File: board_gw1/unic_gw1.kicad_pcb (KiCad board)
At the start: 4 copper layers, 50 x 15.2 mm, 127 parts, among them Q1 2N7002, Q10 2N7002, Q11 2N7002, Q12 2N7002, Q13 2N7002, Q14 2N7002, Q15 2N7002, Q16 2N7002, Q17 2N7002, Q18 2N7002, Q19 2N7002, Q2 2N7002, Q20 2N7002, Q21 2N7002, Q22 2N7002, Q23 2N7002, Q24 2N7002, Q25 2N7002, Q26 2N7002, Q27 2N7002, Q28 2N7002, Q29 2N7002, Q3 2N7002, Q30 2N7002, Q31 2N7002, Q32 2N7002, Q33 2N7002, Q34 2N7002, Q35 2N7002, Q36 2N7002, Q37 2N7002, Q38 2N7002, Q39 2N7002, Q4 2N7002, Q40 2N7002, Q41 2N7002, Q5 2N7002, Q6 2N7002, Q7 2N7002, Q8 2N7002, Q9 2N7002, U1 GW1N-LV9QN88C6_I5_, U3 MIC5203-3.3BM5, U4 APS6404L-3SQR-ZR, U5 MIC5504-1.2YM5, U6 AP62150Z6, U7 W25Q16JVUXIQ, X1 27MHz

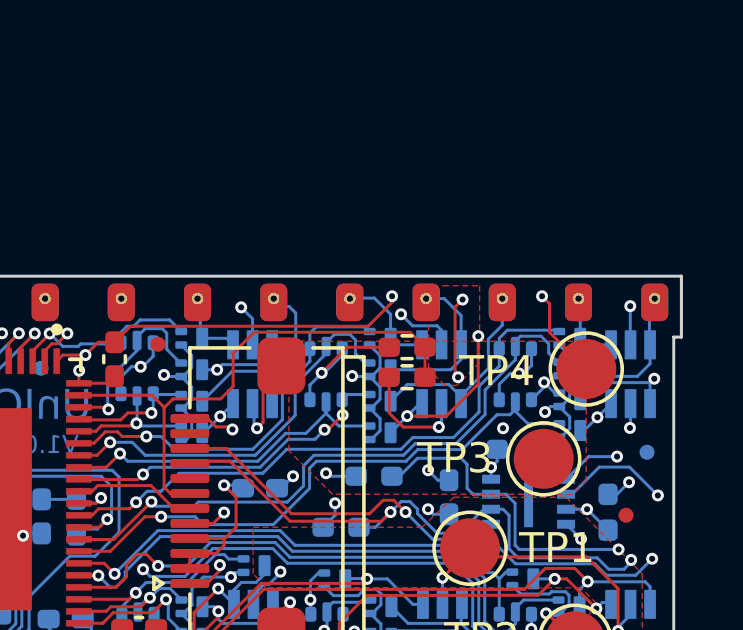
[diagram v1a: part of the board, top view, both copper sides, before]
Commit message: Changed PCB to match that of manufacturing:
1. Removed solder paste from U1 (as it will be hand-soldered).
2. Changed vias to have pads on top/bottom.
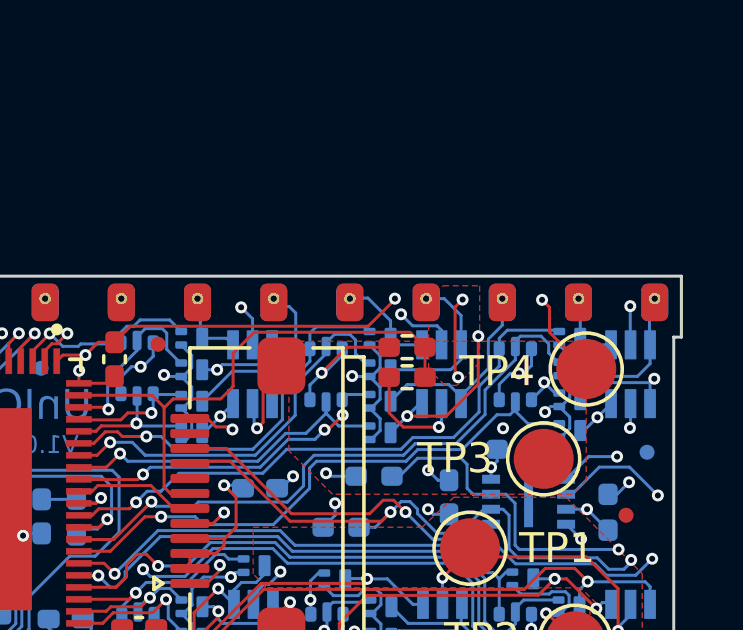
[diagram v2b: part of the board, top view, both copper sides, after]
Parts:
- U1: value GW1N-LV9QN88C6_I5_ -> GW1NR-LV9-QN88-C6/I5

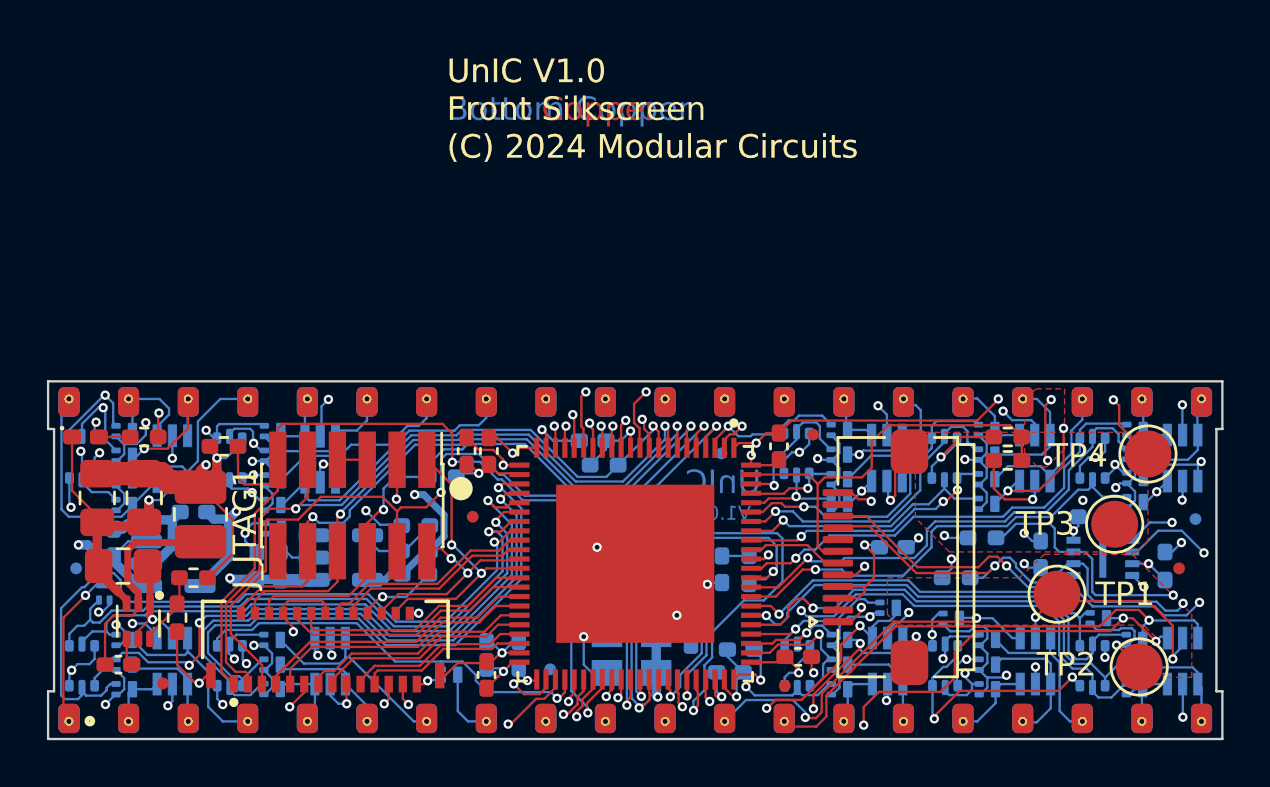
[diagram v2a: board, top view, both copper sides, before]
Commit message: New diodes are added
PCB is also fixed up, but fab notes
need cleaning. Also, I need to select
an actual diode.
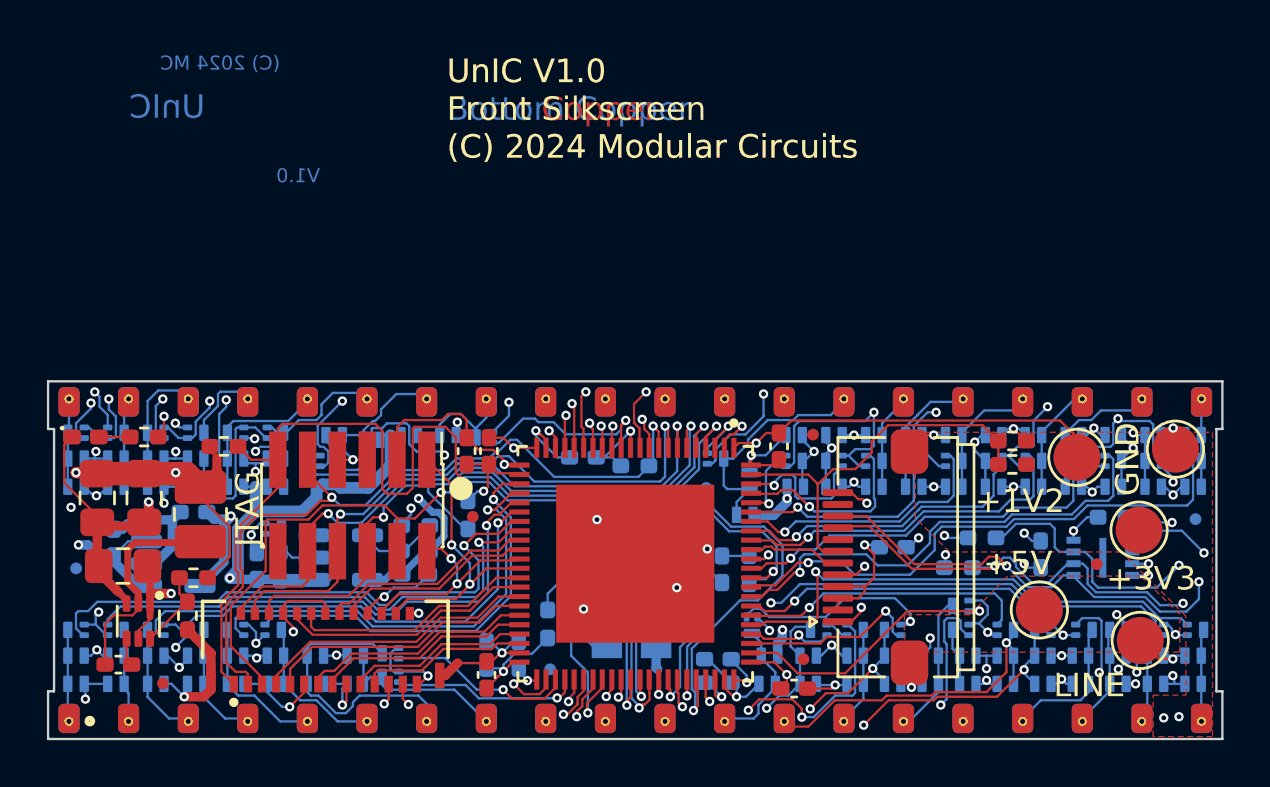
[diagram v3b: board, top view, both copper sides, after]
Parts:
- removed D21, D22, D23, D24, D25, D26, D27, D28, D29, D30: BAT54CV, UNIC:SOT-666
- added D10: D_Schottky, Diode_SMD:D_SOD-882, B.Cu at (70.7, 68.0)
- added D12: D_Schottky, Diode_SMD:D_SOD-882, B.Cu at (70.7, 66.8)
- added D13: D_Schottky, Diode_SMD:D_SOD-882, B.Cu at (46.3, 68.0)
- added D14: D_Schottky, Diode_SMD:D_SOD-882, B.Cu at (48.0, 66.8)
- added D15: D_Schottky, Diode_SMD:D_SOD-882, B.Cu at (48.0, 68.0)
- added D16: D_Schottky, Diode_SMD:D_SOD-882, B.Cu at (80.7, 66.8)
- added D17: D_Schottky, Diode_SMD:D_SOD-882, B.Cu at (80.7, 68.0)
- added D18: D_Schottky, Diode_SMD:D_SOD-882, B.Cu at (79.1, 66.8)
- added D19: D_Schottky, Diode_SMD:D_SOD-882, B.Cu at (79.1, 68.0)
- added D20: D_Schottky, Diode_SMD:D_SOD-882, B.Cu at (87.1, 66.8)
- added D31: D_Schottky, Diode_SMD:D_SOD-882, B.Cu at (87.1, 68.0)
- added D32: D_Schottky, Diode_SMD:D_SOD-882, B.Cu at (85.5, 66.8)
- added D33: D_Schottky, Diode_SMD:D_SOD-882, B.Cu at (85.5, 68.0)
- added D34: D_Schottky, Diode_SMD:D_SOD-882, B.Cu at (74.3, 66.8)
- added D35: D_Schottky, Diode_SMD:D_SOD-882, B.Cu at (74.3, 68.0)
- added D36: D_Schottky, Diode_SMD:D_SOD-882, B.Cu at (70.1, 59.6)
- added D37: D_Schottky, Diode_SMD:D_SOD-882, B.Cu at (70.1, 57.4)
- added D38: D_Schottky, Diode_SMD:D_SOD-882, B.Cu at (87.1, 59.6)
- added D39: D_Schottky, Diode_SMD:D_SOD-882, B.Cu at (87.1, 57.4)
- added D40: D_Schottky, Diode_SMD:D_SOD-882, B.Cu at (72.7, 66.8)
- added D41: D_Schottky, Diode_SMD:D_SOD-882, B.Cu at (72.7, 68.0)
- added D42: D_Schottky, Diode_SMD:D_SOD-882, B.Cu at (44.6, 68.0)
- added D43: D_Schottky, Diode_SMD:D_SOD-882, B.Cu at (42.9, 66.8)
- added D44: D_Schottky, Diode_SMD:D_SOD-882, B.Cu at (42.9, 68.0)
- added D45: D_Schottky, Diode_SMD:D_SOD-882, B.Cu at (69.0, 66.8)
- added D46: D_Schottky, Diode_SMD:D_SOD-882, B.Cu at (68.9, 68.0)
- added D47: D_Schottky, Diode_SMD:D_SOD-882, B.Cu at (85.4, 59.6)
- added D48: D_Schottky, Diode_SMD:D_SOD-882, B.Cu at (85.4, 57.4)
- added D49: D_Schottky, Diode_SMD:D_SOD-882, B.Cu at (46.3, 59.6)
- added D50: D_Schottky, Diode_SMD:D_SOD-882, B.Cu at (46.3, 58.4)
- added D51: D_Schottky, Diode_SMD:D_SOD-882, B.Cu at (48.0, 59.6)
- added D52: D_Schottky, Diode_SMD:D_SOD-882, B.Cu at (48.0, 58.4)
- added D53: D_Schottky, Diode_SMD:D_SOD-882, B.Cu at (83.7, 59.6)
- added D54: D_Schottky, Diode_SMD:D_SOD-882, B.Cu at (83.7, 57.4)
- added D55: D_Schottky, Diode_SMD:D_SOD-882, B.Cu at (83.9, 66.8)
- added D56: D_Schottky, Diode_SMD:D_SOD-882, B.Cu at (83.9, 68.0)
- added D57: D_Schottky, Diode_SMD:D_SOD-882, B.Cu at (41.2, 66.8)
- added D58: D_Schottky, Diode_SMD:D_SOD-882, B.Cu at (41.2, 68.0)
- added D59: D_Schottky, Diode_SMD:D_SOD-882, B.Cu at (51.4, 66.8)
- added D60: D_Schottky, Diode_SMD:D_SOD-882, B.Cu at (51.4, 68.0)
- added D61: D_Schottky, Diode_SMD:D_SOD-882, B.Cu at (82.3, 66.8)
- added D62: D_Schottky, Diode_SMD:D_SOD-882, B.Cu at (82.3, 68.0)
- added D63: D_Schottky, Diode_SMD:D_SOD-882, B.Cu at (75.2, 59.6)
- added D64: D_Schottky, Diode_SMD:D_SOD-882, B.Cu at (75.2, 57.4)
- added D65: D_Schottky, Diode_SMD:D_SOD-882, B.Cu at (52.1, 57.6)
- added D66: D_Schottky, Diode_SMD:D_SOD-882, B.Cu at (50.5, 57.4)
- added D67: D_Schottky, Diode_SMD:D_SOD-882, B.Cu at (53.7, 57.4)
- added D68: D_Schottky, Diode_SMD:D_SOD-882, B.Cu at (55.3, 57.4)
- added D69: D_Schottky, Diode_SMD:D_SOD-882, B.Cu at (76.9, 59.6)
- added D70: D_Schottky, Diode_SMD:D_SOD-882, B.Cu at (76.9, 57.4)
- added D71: D_Schottky, Diode_SMD:D_SOD-882, B.Cu at (77.5, 66.8)
- added D72: D_Schottky, Diode_SMD:D_SOD-882, B.Cu at (77.5, 68.0)
- added D73: D_Schottky, Diode_SMD:D_SOD-882, B.Cu at (49.7, 66.8)
- added D74: D_Schottky, Diode_SMD:D_SOD-882, B.Cu at (49.7, 68.0)
- added D75: D_Schottky, Diode_SMD:D_SOD-882, B.Cu at (80.3, 59.6)
- added D76: D_Schottky, Diode_SMD:D_SOD-882, B.Cu at (80.3, 57.4)
- added D77: D_Schottky, Diode_SMD:D_SOD-882, B.Cu at (41.2, 59.6)
- added D78: D_Schottky, Diode_SMD:D_SOD-882, B.Cu at (41.2, 58.4)
- added D79: D_Schottky, Diode_SMD:D_SOD-882, B.Cu at (42.9, 59.6)
- added D80: D_Schottky, Diode_SMD:D_SOD-882, B.Cu at (42.9, 58.4)
- added D81: D_Schottky, Diode_SMD:D_SOD-882, B.Cu at (44.6, 59.6)
- added D82: D_Schottky, Diode_SMD:D_SOD-882, B.Cu at (44.6, 58.4)
- added D83: D_Schottky, Diode_SMD:D_SOD-882, B.Cu at (68.0, 60.8)
- added D84: D_Schottky, Diode_SMD:D_SOD-882, B.Cu at (68.2, 59.3)
- added D85: D_Schottky, Diode_SMD:D_SOD-882, B.Cu at (78.6, 59.6)
- added D86: D_Schottky, Diode_SMD:D_SOD-882, B.Cu at (78.6, 57.4)
- added D87: D_Schottky, Diode_SMD:D_SOD-882, B.Cu at (71.8, 59.6)
- added D88: D_Schottky, Diode_SMD:D_SOD-882, B.Cu at (71.8, 57.4)
- added D89: D_Schottky, Diode_SMD:D_SOD-882, B.Cu at (39.5, 59.6)
- added D90: D_Schottky, Diode_SMD:D_SOD-882, B.Cu at (39.5, 58.4)
- added TP5: TestPoint, UNIC:TestPoint_Pad_D2.0mm, F.Cu at (86.3, 58.0)
- D1, D11, D2, D3, D4, D5, D6, D7, D8, D9: value BAT54DF -> D_Schottky; footprint UNIC:SOT65P210X110-6N -> Diode_SMD:D_SOD-882
- moved D5 40.4 mm to (46.3, 66.8), turned to 180 degrees
- moved D3 34.6 mm to (39.5, 68.0), turned to 0 degrees
- moved D8 32.1 mm to (82.0, 57.4), turned to 0 degrees
- moved D9 29.9 mm to (73.5, 59.6), turned to 0 degrees
- moved R9 26.4 mm to (59.6, 65.4), turned to 90 degrees
- moved D11 13.2 mm to (73.5, 57.4), turned to 180 degrees
- moved D2 10.8 mm to (39.5, 66.8), turned to 180 degrees
- moved D6 10.6 mm to (75.9, 68.0), turned to 180 degrees
- moved Q36 9.47 mm to (56.9, 57.5), turned to 180 degrees
- moved Q15 8.50 mm to (68.3, 65.5), turned to -90 degrees
- moved D7 8.04 mm to (82.0, 59.6), turned to 180 degrees
- moved Q13 5.74 mm to (77.2, 64.6), turned to 180 degrees
- moved Q16 5.58 mm to (83.9, 65.7), turned to 180 degrees
- moved Q20 5.52 mm to (79.1, 65.7)
- moved Q29 5.42 mm to (66.7, 58.4)
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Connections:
- D1 pad 1: /PIN1 -> LINE
- D1 pad 2: LINE -> /PIN4
- D11 pad 1: /PIN22 -> /PIN26
- D11 pad 2: LINE -> GND
- D2 pad 1: /PIN8 -> LINE
- D2 pad 2: LINE -> /PIN1
- D3 pad 1: /PIN9 -> /PIN1
- D3 pad 2: LINE -> GND
- D4 pad 1: /PIN12 -> LINE
- D4 pad 2: LINE -> /PIN15
- D5 pad 1: /PIN11 -> LINE
- D5 pad 2: LINE -> /PIN5
- D6 pad 1: /PIN25 -> /PIN15
- D6 pad 2: LINE -> GND
- D7 pad 1: /PIN27 -> LINE
- D7 pad 2: LINE -> /PIN22
- D8 pad 1: /PIN36 -> /PIN22
- D8 pad 2: LINE -> GND
- D9 pad 1: /PIN39 -> LINE
- D9 pad 2: LINE -> /PIN26
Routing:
- net +5V: track 57.5 -> 82.5 mm, vias 15 -> 20
- net +3V3: track 85.4 -> 61.8 mm, vias 29 -> 19
- net GND: track 81.5 -> 100.8 mm, vias 37 -> 44
- net /PIN33_F: track 21.2 -> 7.98 mm, vias 2 -> 1
- net /PIN12: track 16.7 -> 5.66 mm, vias 2 -> 0
- net /PIN7_F: track 18.0 -> 7.61 mm, vias 2 -> 1
- net /PIN8_F: track 17.8 -> 8.02 mm
- net /PIN2_F: track 30.9 -> 21.2 mm
- net /PIN18_F: track 21.6 -> 30.7 mm
- net /PIN12_F: track 22.0 -> 13.0 mm
- net /PIN13: track 21.8 -> 14.0 mm
- net /PIN17_F: track 19.8 -> 27.5 mm
- net /PIN27: track 2.28 -> 9.86 mm
- net /PIN13_F: track 19.7 -> 12.3 mm
- net /PIN6_F: track 24.8 -> 17.5 mm
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- added copper zone on F.Cu, net +5V
- removed copper zone on F.Cu, net LINE
- removed copper zone on In1.Cu, net LINE
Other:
- board text added: "+1V2"
- board text added: "+3V3"
- board text added: "+5V"
- board text added: "GND"
- board text added: "JTAG"
- board text added: "LINE"

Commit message: Updated diode part and footprint.
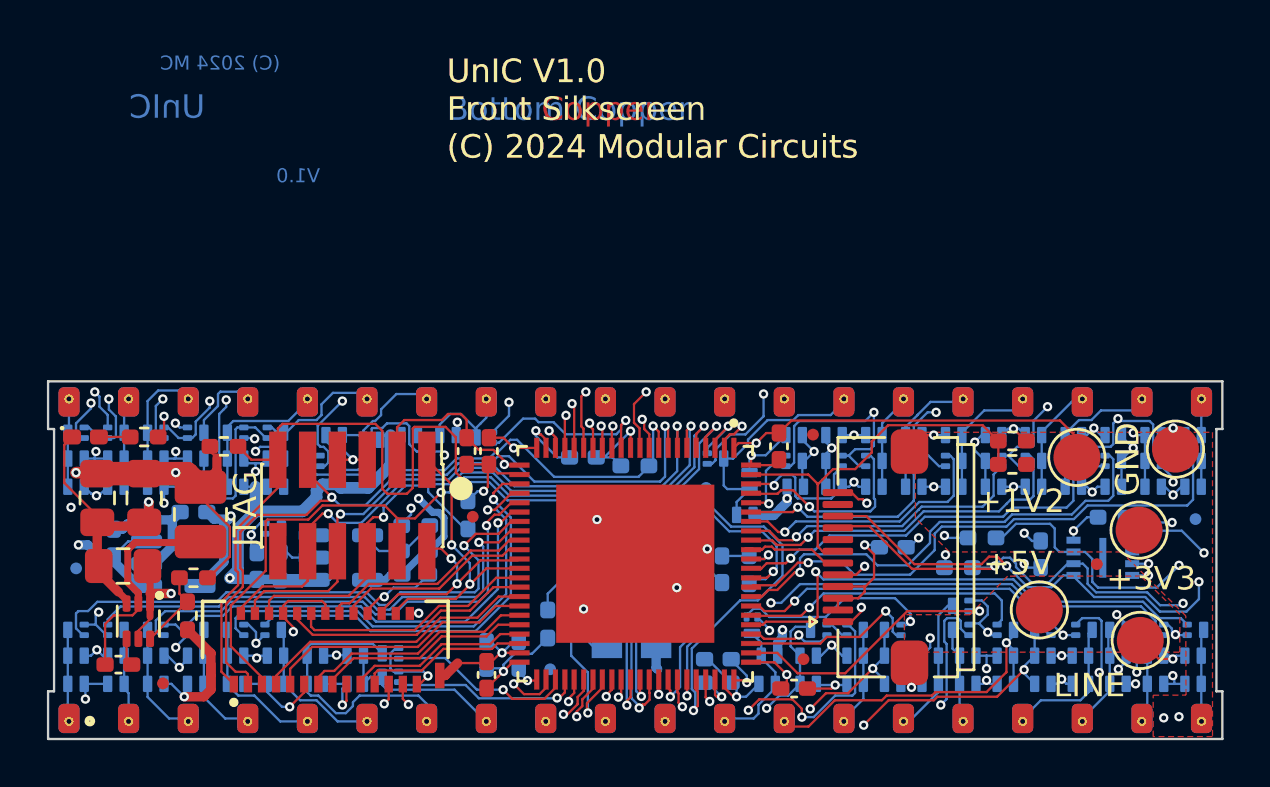
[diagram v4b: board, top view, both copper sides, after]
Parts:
- D1, D10, D11, D12, D13, D14, D15, D16, D17, D18, D19, D2, D20, D3, D31, D32, D33, D34, D35, D36, D37, D38, D39, D4, D40, D41, D42, D43, D44, D45, D46, D47, D48, D49, D5, D50, D51, D52, D53, D54, D55, D56, D57, D58, D59, D6, D60, D61, D62, D63, D64, D65, D66, D67, D68, D69, D7, D70, D71, D72, D73, D74, D75, D76, D77, D78, D79, D8, D80, D81, D82, D83, D84, D85, D86, D87, D88, D89, D9, D90: value D_Schottky -> SM5819L2; footprint Diode_SMD:D_SOD-882 -> UNIC:D_SOD-882
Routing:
- net /PIN16: track 2.64 -> 3.96 mm
